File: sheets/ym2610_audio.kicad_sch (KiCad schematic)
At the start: 51 parts, among them J3 SMK S-G8043, U25 NJM2016D, U26 YM3016D, U27 YM2610, U28 RC4558, U29 RC4558, U30 RC4558, U31 RC4558

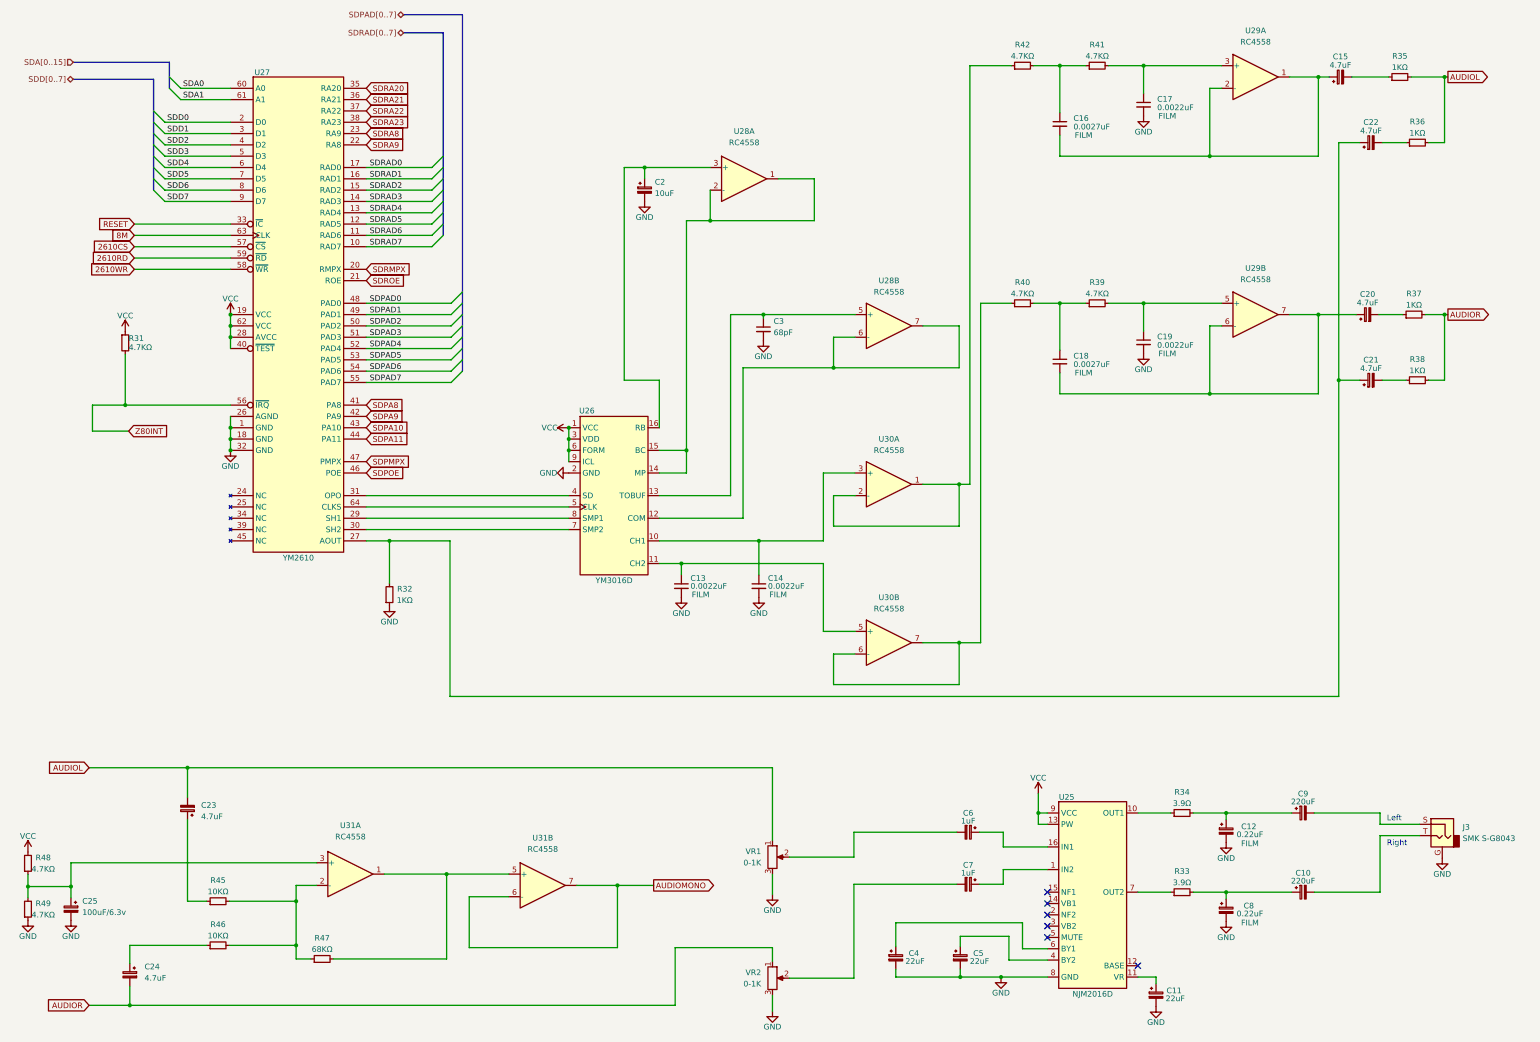
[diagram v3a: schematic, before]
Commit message: Corrected the PC4741, The original schematics does not match the board for the audio circuit, still requires more changes as the board is laid out
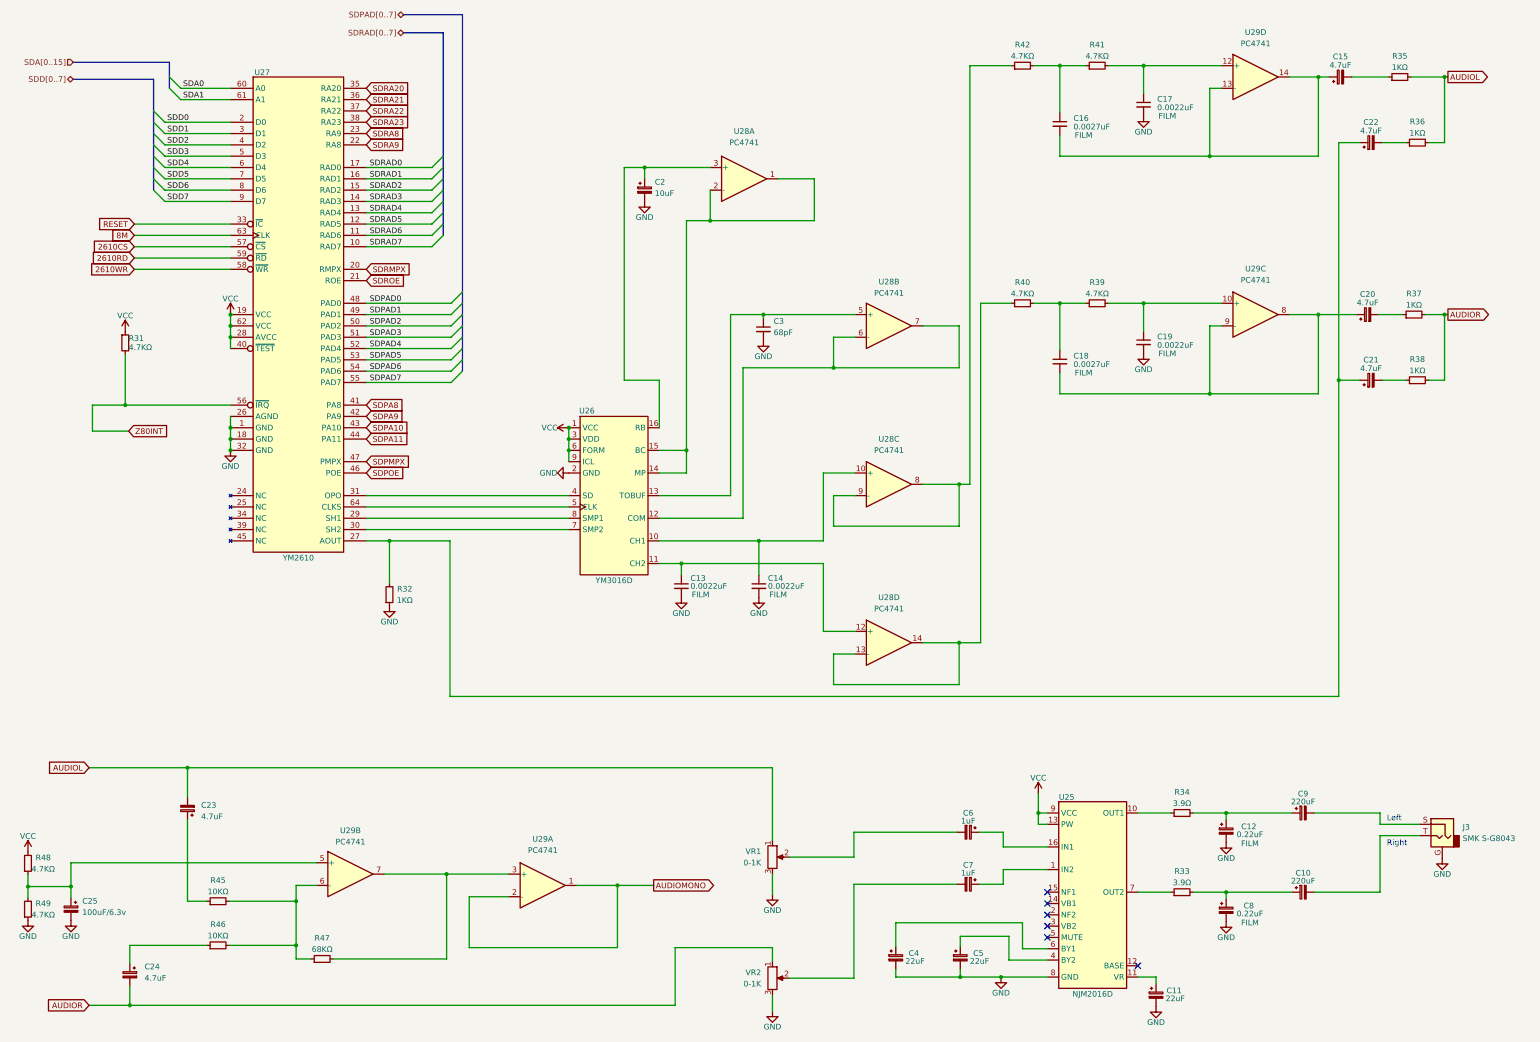
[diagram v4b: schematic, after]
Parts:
- removed U28, U29, U30, U31: RC4558, Package_DIP:DIP-8_W7.62mm, symbol Amplifier_Operational:RC4558
- added U28, U29: PC4741, Package_DIP:DIP-14_W7.62mm, symbol Amplifier_Operational:LM324
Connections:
- net AUDIOMONO: now also U29.1, U29.2 (-)
- net at R45.2, R46.2, R47.1: now also U29.6 (-)
- net at C13.1, U26.11 (CH2): now also U28.12 (+)
- net at C18.2, C20.1: now also U29.8, U29.9 (-)
- net at C3.1, U26.13 (TOBUF): now also U28.5 (+)
- net at U26.12 (COM): now also U28.6 (-), U28.7
- net at R42.1: now also U28.8, U28.9 (-)
- net at C14.1, U26.10 (CH1): now also U28.10 (+)
- net at C17.1, R41.2: now also U29.12 (+)
- net at R47.2: now also U29.3 (+), U29.7
- net at C15.1, C16.2: now also U29.13 (-), U29.14
- net at R40.1: now also U28.13 (-), U28.14
- net at C2.1, U26.16 (RB): now also U28.3 (+)
- net at U26.14 (MP), U26.15 (BC): now also U28.1, U28.2 (-)
- net at C19.1, R39.2: now also U29.10 (+)
- net at C25.1, R48.1, R49.2: now also U29.5 (+)

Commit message: Some Audio Changes C13 C14
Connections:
- net GND: no longer C13.2, C14.2
- net at U26.14 (MP), U26.15 (BC), U28.1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: now also C13.2
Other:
- moved on the sheet: C13, C14
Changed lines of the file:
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@@
   (junction (at 256.794 122.301) (diameter 0) (color 0 0 0 0)
   )
+  (junction (at 226.314 119.761) (diameter 0) (color 0 0 0 0)
+  )
   (junction (at 313.055 101.981) (diameter 0) (color 0 0 0 0)
   )
@@
   (junction (at 279.4 28.321) (diameter 0) (color 0 0 0 0)
   )
+  (junction (at 195.58 119.761) (diameter 0) (color 0 0 0 0)
+  )
   (junction (at 195.58 114.681) (diameter 0) (color 0 0 0 0)
   )
@@
   (junction (at 298.196 28.321) (diameter 0) (color 0 0 0 0)
   )
-  (junction (at 194.437 140.081) (diameter 0) (color 0 0 0 0)
+  (junction (at 202.692 140.081) (diameter 0) (color 0 0 0 0)
   )
   (junction (at 256.794 157.861) (diameter 0) (color 0 0 0 0)
@@
   (junction (at 93.218 86.741) (diameter 0) (color 0 0 0 0)
   )
-  (junction (at 211.836 135.001) (diameter 0) (color 0 0 0 0)
-  )
   (junction (at 186.182 51.181) (diameter 0) (color 0 0 0 0)
   )
   (junction (at 365.76 30.861) (diameter 0) (color 0 0 0 0)
+  )
+  (junction (at 195.58 110.617) (diameter 0) (color 0 0 0 0)
   )
   (junction (at 141.732 209.804) (diameter 0) (color 0 0 0 0)
@@
     (stroke (width 0) (type default) (color 0 0 0 0))
   )
-  (wire (pts (xy 189.484 135.001) (xy 211.836 135.001))
+  (wire (pts (xy 189.484 135.001) (xy 226.314 135.001))
     (stroke (width 0) (type default) (color 0 0 0 0))
   )
@@
     (stroke (width 0) (type default) (color 0 0 0 0))
   )
-  (wire (pts (xy 194.437 140.081) (xy 226.314 140.081))
-    (stroke (width 0) (type default) (color 0 0 0 0))
-  )
   (wire (pts (xy 212.852 84.201) (xy 212.852 84.963))
     (stroke (width 0) (type default) (color 0 0 0 0))
@@
     (stroke (width 0) (type default) (color 0 0 0 0))
   )
-  (wire (pts (xy 189.484 140.081) (xy 194.437 140.081))
+  (wire (pts (xy 189.484 140.081) (xy 202.692 140.081))
     (stroke (width 0) (type default) (color 0 0 0 0))
   )
@@
     (stroke (width 0) (type default) (color 0 0 0 0))
   )
+  (wire (pts (xy 195.58 142.621) (xy 195.58 119.761))
+    (stroke (width 0) (type default) (color 0 0 0 0))
+  )
   (wire (pts (xy 78.486 46.101) (xy 93.218 46.101))
     (stroke (width 0) (type default) (color 0 0 0 0))
@@
     (stroke (width 0) (type default) (color 0 0 0 0))
   )
-  (wire (pts (xy 195.58 114.681) (xy 195.58 63.119))
+  (wire (pts (xy 195.58 114.681) (xy 195.58 110.617))
     (stroke (width 0) (type default) (color 0 0 0 0))
   )
@@
     (stroke (width 0) (type default) (color 0 0 0 0))
   )
+  (wire (pts (xy 226.314 114.554) (xy 226.314 110.617))
+    (stroke (width 0) (type default) (color 0 0 0 0))
+  )
   (wire (pts (xy 279.4 81.661) (xy 279.4 92.202))
     (stroke (width 0) (type default) (color 0 0 0 0))
@@
     (stroke (width 0) (type default) (color 0 0 0 0))
   )
+  (wire (pts (xy 202.692 140.081) (xy 226.314 140.081))
+    (stroke (width 0) (type default) (color 0 0 0 0))
+  )
   (wire (pts (xy 233.426 160.401) (xy 228.6 160.401))
     (stroke (width 0) (type default) (color 0 0 0 0))
@@
     (stroke (width 0) (type default) (color 0 0 0 0))
   )
+  (wire (pts (xy 195.58 110.617) (xy 195.58 63.119))
+    (stroke (width 0) (type default) (color 0 0 0 0))
+  )
   (bus (pts (xy 140.97 56.261) (xy 140.97 53.721))
     (stroke (width 0) (type default) (color 0 0 0 0))
@@
     (stroke (width 0) (type default) (color 0 0 0 0))
   )
+  (wire (pts (xy 197.612 142.621) (xy 195.58 142.621))
+    (stroke (width 0) (type default) (color 0 0 0 0))
+  )
   (wire (pts (xy 226.314 140.081) (xy 226.314 155.321))
     (stroke (width 0) (type default) (color 0 0 0 0))
@@
     (stroke (width 0) (type default) (color 0 0 0 0))
   )
-  (wire (pts (xy 211.836 135.001) (xy 211.836 142.621))
-    (stroke (width 0) (type default) (color 0 0 0 0))
-  )
   (wire (pts (xy 169.164 112.141) (xy 169.164 114.681))
     (stroke (width 0) (type default) (color 0 0 0 0))
@@
     (stroke (width 0) (type default) (color 0 0 0 0))
   )
-  (wire (pts (xy 194.437 140.081) (xy 194.437 142.621))
+  (wire (pts (xy 202.692 140.081) (xy 202.692 142.621))
     (stroke (width 0) (type default) (color 0 0 0 0))
   )
@@
     (stroke (width 0) (type default) (color 0 0 0 0))
   )
+  (wire (pts (xy 226.314 110.617) (xy 195.58 110.617))
+    (stroke (width 0) (type default) (color 0 0 0 0))
+  )
   (wire (pts (xy 266.192 232.918) (xy 257.048 232.918))
     (stroke (width 0) (type default) (color 0 0 0 0))
@@
   )
   (wire (pts (xy 123.698 81.661) (xy 142.748 81.661))
-    (stroke (width 0) (type default) (color 0 0 0 0))
-  )
-  (wire (pts (xy 211.836 135.001) (xy 226.314 135.001))
     (stroke (width 0) (type default) (color 0 0 0 0))
   )
@@
     (pin "2")
   )
-  (symbol (lib_id "Device:C_Small") (at 194.437 145.161 0) (unit 1)
-    (in_bom yes) (on_board yes)
-    (property "Reference" "C13" (id 0) (at 196.469 143.383 0)
-      (effects (font (size 1.27 1.27)) (justify left))
-    )
-    (property "Value" "0.0022uF" (id 1) (at 196.469 145.161 0)
-      (effects (font (size 1.27 1.27)) (justify left))
-    )
-    (property "Footprint" "1_NeoGeoLibrary:CAP3-5mm" (id 2) (at 194.437 145.161 0)
-      (effects (font (size 1.27 1.27)) hide)
-    )
-    (property "Datasheet" "" (id 3) (at 194.437 145.161 0)
-      (effects (font (size 1.27 1.27)) hide)
-    )
-    (property "Type" "FILM" (id 4) (at 198.755 147.066 0))
+  (symbol (lib_id "Device:C_Small") (at 200.152 142.621 270) (unit 1)
+    (in_bom yes) (on_board yes)
+    (property "Reference" "C13" (id 0) (at 200.152 145.669 90))
+    (property "Value" "0.0022uF" (id 1) (at 200.152 147.574 90))
+    (property "Footprint" "1_NeoGeoLibrary:CAP3-5mm" (id 2) (at 200.152 142.621 0)
+      (effects (font (size 1.27 1.27)) hide)
+    )
+    (property "Datasheet" "" (id 3) (at 200.152 142.621 0)
+      (effects (font (size 1.27 1.27)) hide)
+    )
+    (property "Type" "FILM" (id 4) (at 200.152 149.479 90))
     (pin "1")
     (pin "2")
@@
     (pin "1")
   )
-  (symbol (lib_id "power:GND") (at 194.437 147.701 0) (unit 1)
-    (in_bom yes) (on_board yes)
-    (property "Reference" "#PWR0202" (id 0) (at 194.437 154.051 0)
-      (effects (font (size 1.27 1.27)) hide)
-    )
-    (property "Value" "GND" (id 1) (at 194.437 151.257 0))
-    (property "Footprint" "" (id 2) (at 194.437 147.701 0)
-      (effects (font (size 1.27 1.27)) hide)
-    )
-    (property "Datasheet" "" (id 3) (at 194.437 147.701 0)
-      (effects (font (size 1.27 1.27)) hide)
-    )
-    (pin "1")
-  )
   (symbol (lib_id "power:VCC") (at 93.218 84.201 0) (unit 1)
     (in_bom yes) (on_board yes)
@@
     (pin "1")
   )
-  (symbol (lib_id "power:GND") (at 211.836 147.701 0) (unit 1)
-    (in_bom yes) (on_board yes)
-    (property "Reference" "#PWR0201" (id 0) (at 211.836 154.051 0)
-      (effects (font (size 1.27 1.27)) hide)
-    )
-    (property "Value" "GND" (id 1) (at 211.836 151.257 0))
-    (property "Footprint" "" (id 2) (at 211.836 147.701 0)
-      (effects (font (size 1.27 1.27)) hide)
-    )
-    (property "Datasheet" "" (id 3) (at 211.836 147.701 0)
-      (effects (font (size 1.27 1.27)) hide)
-    )
-    (pin "1")
-  )
   (symbol (lib_id "power:VCC") (at 169.164 109.601 90) (unit 1)
     (in_bom yes) (on_board yes)
@@
     (pin "2")
   )
-  (symbol (lib_id "Device:C_Small") (at 211.836 145.161 0) (unit 1)
-    (in_bom yes) (on_board yes)
-    (property "Reference" "C14" (id 0) (at 213.868 143.383 0)
+  (symbol (lib_id "Device:C_Small") (at 226.314 117.221 180) (unit 1)
+    (in_bom yes) (on_board yes)
+    (property "Reference" "C14" (id 0) (at 224.282 118.999 0)
       (effects (font (size 1.27 1.27)) (justify left))
     )
-    (property "Value" "0.0022uF" (id 1) (at 213.868 145.161 0)
+    (property "Value" "0.0022uF" (id 1) (at 224.282 117.221 0)
       (effects (font (size 1.27 1.27)) (justify left))
     )
-    (property "Footprint" "1_NeoGeoLibrary:CAP3-5mm" (id 2) (at 211.836 145.161 0)
-      (effects (font (size 1.27 1.27)) hide)
-    )
-    (property "Datasheet" "" (id 3) (at 211.836 145.161 0)
-      (effects (font (size 1.27 1.27)) hide)
-    )
-    (property "Type" "FILM" (id 4) (at 216.154 147.066 0))
-    (pin "1")
-    (pin "2")
+    (property "Footprint" "1_NeoGeoLibrary:CAP3-5mm" (id 2) (at 226.314 117.221 0)
+      (effects (font (size 1.27 1.27)) hide)
+    )
+    (property "Datasheet" "" (id 3) (at 226.314 117.221 0)
+      (effects (font (size 1.27 1.27)) hide)
+    )
+    (property "Type" "FILM" (id 4) (at 221.996 115.316 0))
+    (pin "1")
+    (pin "2")

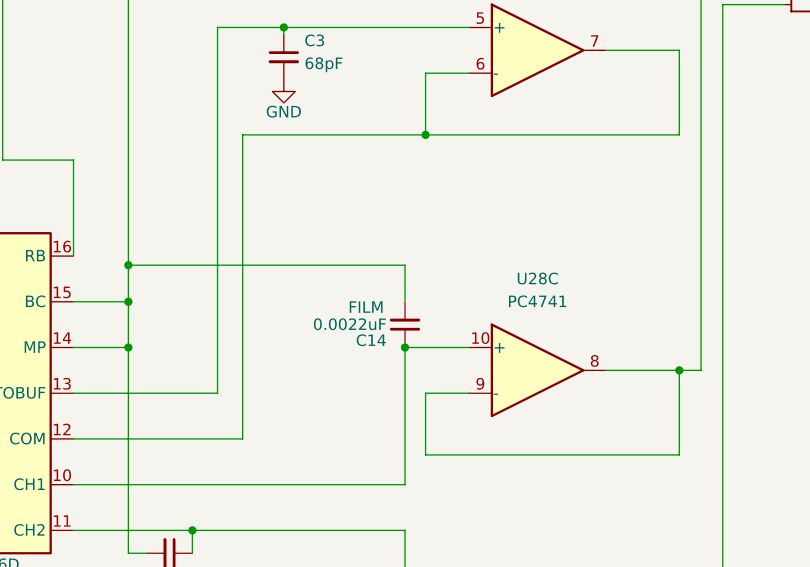
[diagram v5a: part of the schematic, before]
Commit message: C14 track as slightly off
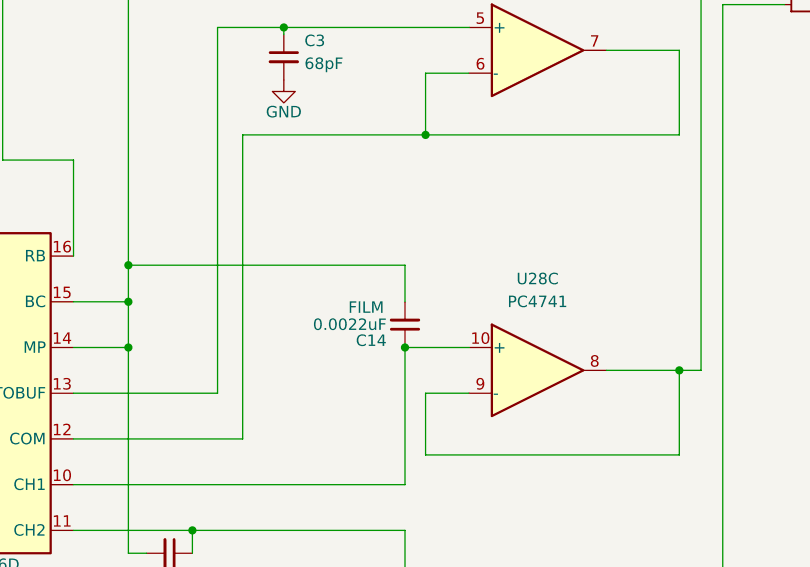
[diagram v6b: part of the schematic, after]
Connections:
- net at C13.2, U26.14 (MP), U26.15 (BC)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: now also C14.2
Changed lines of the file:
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@@
     (stroke (width 0) (type default) (color 0 0 0 0))
   )
-  (wire (pts (xy 226.314 114.554) (xy 226.314 110.617))
+  (wire (pts (xy 226.314 110.617) (xy 226.314 114.681))
     (stroke (width 0) (type default) (color 0 0 0 0))
   )

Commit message: More Audio Changes
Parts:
- added C201: 10uF, 1_NeoGeoLibrary:CAP1-5mm, symbol Device:C_Polarized_Small
- added R201: 1KΩ, 1_NeoGeoLibrary:Resistor1-5mm, symbol Device:R_Small
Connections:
- net at C13.2, C14.2, U26.14 (MP)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: now also R201.1
- net at C21.1, C22.1, R32.2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: now also C201.2
- new net: C201.1, R201.2
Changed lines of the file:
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@@
   (junction (at 226.314 119.761) (diameter 0) (color 0 0 0 0)
   )
+  (junction (at 142.494 135.001) (diameter 0) (color 0 0 0 0)
+  )
   (junction (at 313.055 101.981) (diameter 0) (color 0 0 0 0)
   )
@@
   )
   (junction (at 195.58 110.617) (diameter 0) (color 0 0 0 0)
+  )
+  (junction (at 224.282 53.721) (diameter 0) (color 0 0 0 0)
   )
   (junction (at 141.732 209.804) (diameter 0) (color 0 0 0 0)
@@
     (stroke (width 0) (type default) (color 0 0 0 0))
   )
+  (wire (pts (xy 154.559 38.735) (xy 233.426 38.735))
+    (stroke (width 0) (type default) (color 0 0 0 0))
+  )
   (wire (pts (xy 93.218 104.521) (xy 69.596 104.521))
     (stroke (width 0) (type default) (color 0 0 0 0))
@@
     (stroke (width 0) (type default) (color 0 0 0 0))
   )
+  (wire (pts (xy 233.426 53.086) (xy 233.426 53.721))
+    (stroke (width 0) (type default) (color 0 0 0 0))
+  )
   (wire (pts (xy 71.628 71.501) (xy 93.218 71.501))
     (stroke (width 0) (type default) (color 0 0 0 0))
@@
     (stroke (width 0) (type default) (color 0 0 0 0))
   )
+  (wire (pts (xy 229.362 53.721) (xy 233.426 53.721))
+    (stroke (width 0) (type default) (color 0 0 0 0))
+  )
   (wire (pts (xy 228.6 96.139) (xy 256.794 96.139))
     (stroke (width 0) (type default) (color 0 0 0 0))
@@
     (stroke (width 0) (type default) (color 0 0 0 0))
   )
+  (wire (pts (xy 142.494 135.001) (xy 154.559 135.001))
+    (stroke (width 0) (type default) (color 0 0 0 0))
+  )
   (wire (pts (xy 138.43 63.881) (xy 123.698 63.881))
     (stroke (width 0) (type default) (color 0 0 0 0))
@@
     (stroke (width 0) (type default) (color 0 0 0 0))
   )
+  (wire (pts (xy 233.426 38.735) (xy 233.426 48.006))
+    (stroke (width 0) (type default) (color 0 0 0 0))
+  )
   (bus (pts (xy 75.946 46.101) (xy 75.946 43.561))
     (stroke (width 0) (type default) (color 0 0 0 0))
@@
   )
   (wire (pts (xy 189.484 98.933) (xy 181.61 98.933))
+    (stroke (width 0) (type default) (color 0 0 0 0))
+  )
+  (wire (pts (xy 154.559 135.001) (xy 154.559 38.735))
     (stroke (width 0) (type default) (color 0 0 0 0))
   )
@@
     (pin "11")
     (pin "4")
+  )
+  (symbol (lib_id "Device:C_Polarized_Small") (at 233.426 50.546 0) (mirror x) (unit 1)
+    (in_bom yes) (on_board yes) (fields_autoplaced)
+    (property "Reference" "C201" (id 0) (at 236.22 52.3622 0)
+      (effects (font (size 1.27 1.27)) (justify left))
+    )
+    (property "Value" "10uF" (id 1) (at 236.22 49.8222 0)
+      (effects (font (size 1.27 1.27)) (justify left))
+    )
+    (property "Footprint" "1_NeoGeoLibrary:CAP1-5mm" (id 2) (at 233.426 50.546 0)
+      (effects (font (size 1.27 1.27)) hide)
+    )
+    (property "Datasheet" "" (id 3) (at 233.426 50.546 0)
+      (effects (font (size 1.27 1.27)) hide)
+    )
+    (pin "1")
+    (pin "2")
   )
   (symbol (lib_id "Device:C_Polarized_Small") (at 258.826 200.406 270) (unit 1)
@@
       (effects (font (size 1.27 1.27)) hide)
     )
+    (pin "1")
+    (pin "2")
+  )
+  (symbol (lib_id "Device:R_Small") (at 226.822 53.721 90) (unit 1)
+    (in_bom yes) (on_board yes)
+    (property "Reference" "R201" (id 0) (at 226.822 49.022 90))
+    (property "Value" "1KΩ" (id 1) (at 226.822 51.562 90))
+    (property "Footprint" "1_NeoGeoLibrary:Resistor1-5mm" (id 2) (at 226.822 53.721 0)
+      (effects (font (size 1.27 1.27)) hide)
+    )
+    (property "Datasheet" "" (id 3) (at 226.822 53.721 0)
+      (effects (font (size 1.27 1.27)) hide)
+    )
